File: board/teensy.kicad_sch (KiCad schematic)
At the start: 1 part, among them U2 Teensy4.1_DEV-16771

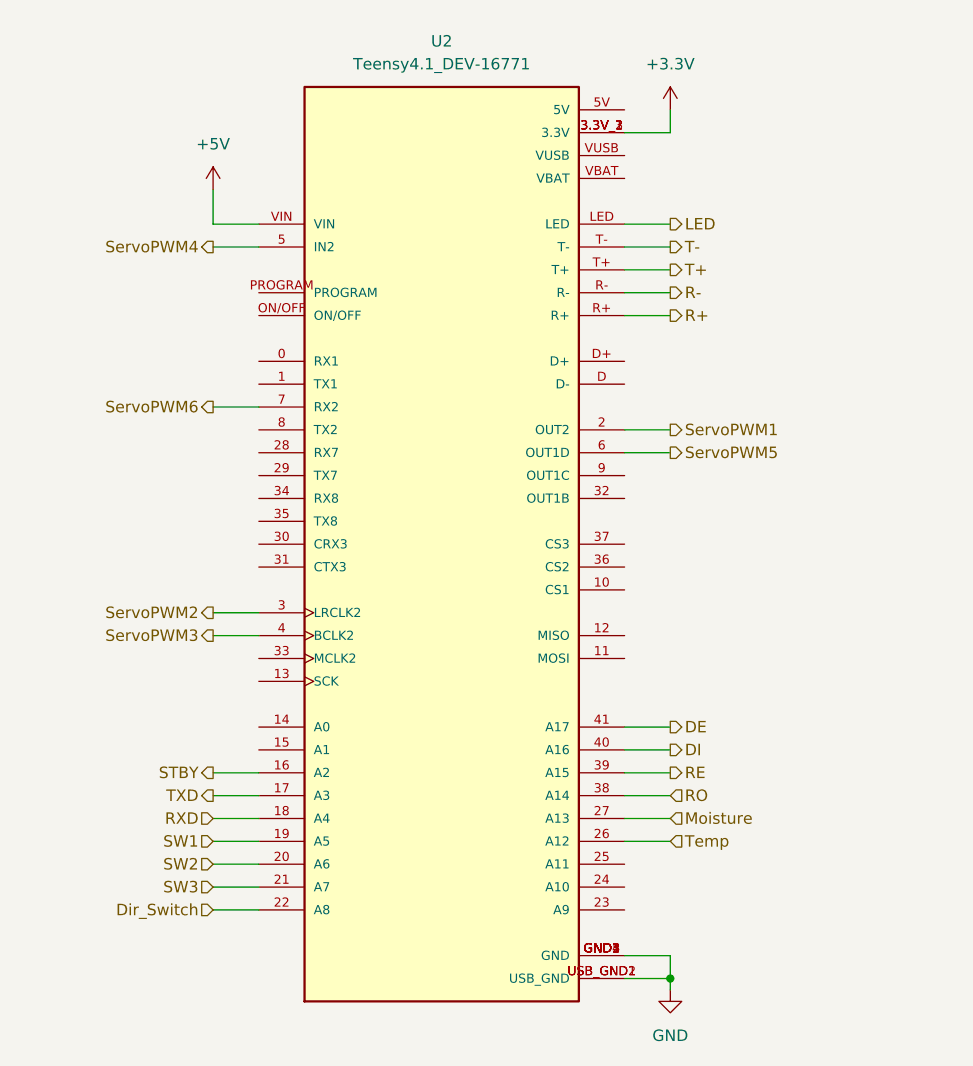
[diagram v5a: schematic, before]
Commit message: Added Labels, Missing Requirements, and Refined Look
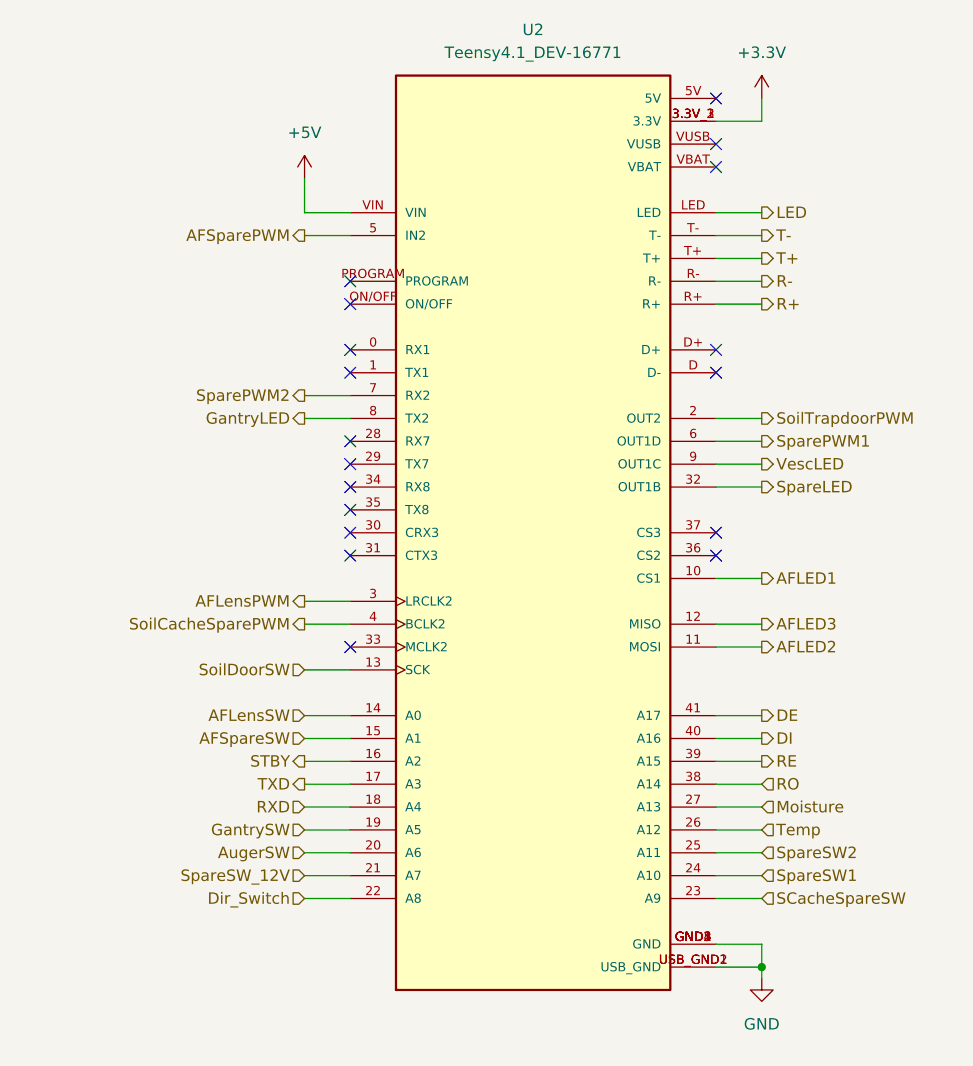
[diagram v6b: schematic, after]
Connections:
- net AFLED1: now reaches U2.10 (CS1)
- net AFLED2: now reaches U2.11 (MOSI)
- net AFLED3: now reaches U2.12 (MISO)
- net SoilDoorSW: now reaches U2.13 (SCK)
- net AFLensSW: now reaches U2.14 (A0)
- net AFSpareSW: now reaches U2.15 (A1)
- net SCacheSpareSW: now reaches U2.23 (A9)
- net SpareSW1: now reaches U2.24 (A10)
- net SpareSW2: now reaches U2.25 (A11)
- net SpareLED: now reaches U2.32 (OUT1B)
- net GantryLED: now reaches U2.8 (TX2)
- net VescLED: now reaches U2.9 (OUT1C)
- net SW1 renamed GantrySW
- net SW2 renamed AugerSW
- net SW3 renamed SpareSW_12V
- net ServoPWM1 renamed SoilTrapdoorPWM
- net ServoPWM2 renamed AFLensPWM
- net ServoPWM3 renamed SoilCacheSparePWM
- net ServoPWM4 renamed AFSparePWM
- net ServoPWM5 renamed SparePWM1
- net ServoPWM6 renamed SparePWM2
- no-connect marks 0 -> 18
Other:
- moved on the sheet: U2

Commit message: Adjusted resistor values & renamed AF outputs
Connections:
- net AFLED1 renamed AFLED340
- net AFLED2 renamed AFLED490
- net AFLED3 renamed AFLED405
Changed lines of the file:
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@@
 		)
 	)
-	(hierarchical_label "AFLED3"
+	(hierarchical_label "AFLED405"
 		(shape output)
 		(at 170.18 99.06 0)
@@
 		)
 	)
-	(hierarchical_label "AFLED2"
+	(hierarchical_label "AFLED490"
 		(shape output)
 		(at 170.18 101.6 0)
@@
 		)
 	)
-	(hierarchical_label "AFLED1"
+	(hierarchical_label "AFLED340"
 		(shape output)
 		(at 170.18 93.98 0)

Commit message: Added Extra 5V out from teensy
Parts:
- U2: footprint MODULE_DEV-16771 -> MRDT_Shields:Teensy_4_1_Ethernet
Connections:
- net +5V: now also U2.5V
- no-connect marks 18 -> 17
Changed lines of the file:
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@@
-	)
-	(no_connect
-		(at 165.1 40.64)
 	)
 	(no_connect
@@
 	(wire
 		(pts
+			(xy 165.1 40.64) (xy 166.37 40.64)
+		)
+		(stroke
+			(width 0)
+			(type default)
+		)
+	)
+	(wire
+		(pts
 			(xy 165.1 109.22) (xy 170.18 109.22)
 		)
@@
 		(pts
 			(xy 165.1 101.6) (xy 170.18 101.6)
+		)
+		(stroke
+			(width 0)
+			(type default)
+		)
+	)
+	(wire
+		(pts
+			(xy 166.37 40.64) (xy 166.37 38.1)
 		)
 		(stroke
@@
 			)
 		)
-		(property "Footprint" "MODULE_DEV-16771"
+		(property "Footprint" "MRDT_Shields:Teensy_4_1_Ethernet"
 			(at 198.12 96.52 0)
 			(effects
@@
 					(unit 1)
 				)
+			)
+		)
+	)
+	(symbol
+		(lib_id "power:+5V")
+		(at 166.37 38.1 0)
+		(unit 1)
+		(exclude_from_sim no)
+		(in_bom yes)
+		(on_board yes)
+		(dnp no)
+		(fields_autoplaced yes)
+		(property "Reference" "#PWR064"
+			(at 166.37 41.91 0)
+			(effects
+				(font
+					(size 1.27 1.27)
+				)
+				(hide yes)
+			)
+		)
+		(property "Value" "+5V"
+			(at 166.37 33.02 0)
+			(effects
+				(font
+					(size 1.27 1.27)
+				)
+			)
+		)
+		(property "Footprint" ""
+			(at 166.37 38.1 0)
+			(effects
+				(font
+					(size 1.27 1.27)
+				)
+				(hide yes)
+			)
+		)
+		(property "Datasheet" ""
+			(at 166.37 38.1 0)
+			(effects
+				(font
+					(size 1.27 1.27)
+				)
+				(hide yes)
+			)
+		)
+		(property "Description" "Power symbol creates a global label with name \"+5V\""
+			(at 166.37 38.1 0)
+			(effects
+				(font
+					(size 1.27 1.27)
+				)
+				(hide yes)
+			)
+		)
+		(pin "1"
+		)
+		(instances
+			(project "AugerBoard"
+				(path "/05fd3c2e-b986-4426-9c38-2a77d5c929de/23b17310-6f85-4d9a-8e16-579a52ef7695"
+					(reference "#PWR064")
+					(unit 1)
+				)
